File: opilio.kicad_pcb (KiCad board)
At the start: 4 copper layers, 74.9 x 40 mm, 92 parts, among them J1 Screw_Terminal_01x02, J2 USB_C_Receptacle_USB2.0, J3 Conn_01x02_Male, J4 Conn_01x02_Male, J5 Conn_01x02_Male, Q1 PMV25ENEAR, Q2 AO3401A, SW1 Reset, SW2 Boot, U1 EUP3458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

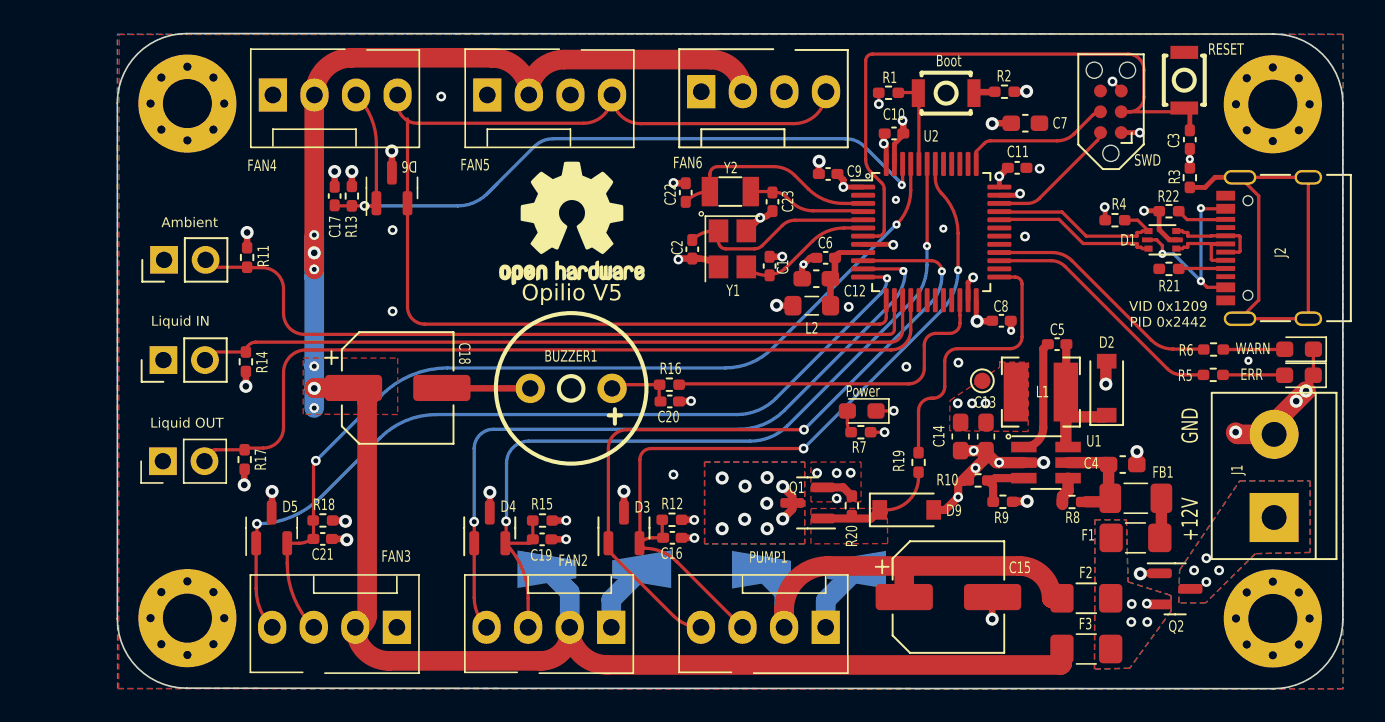
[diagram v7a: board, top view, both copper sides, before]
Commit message: v6 with P-channel mosfet
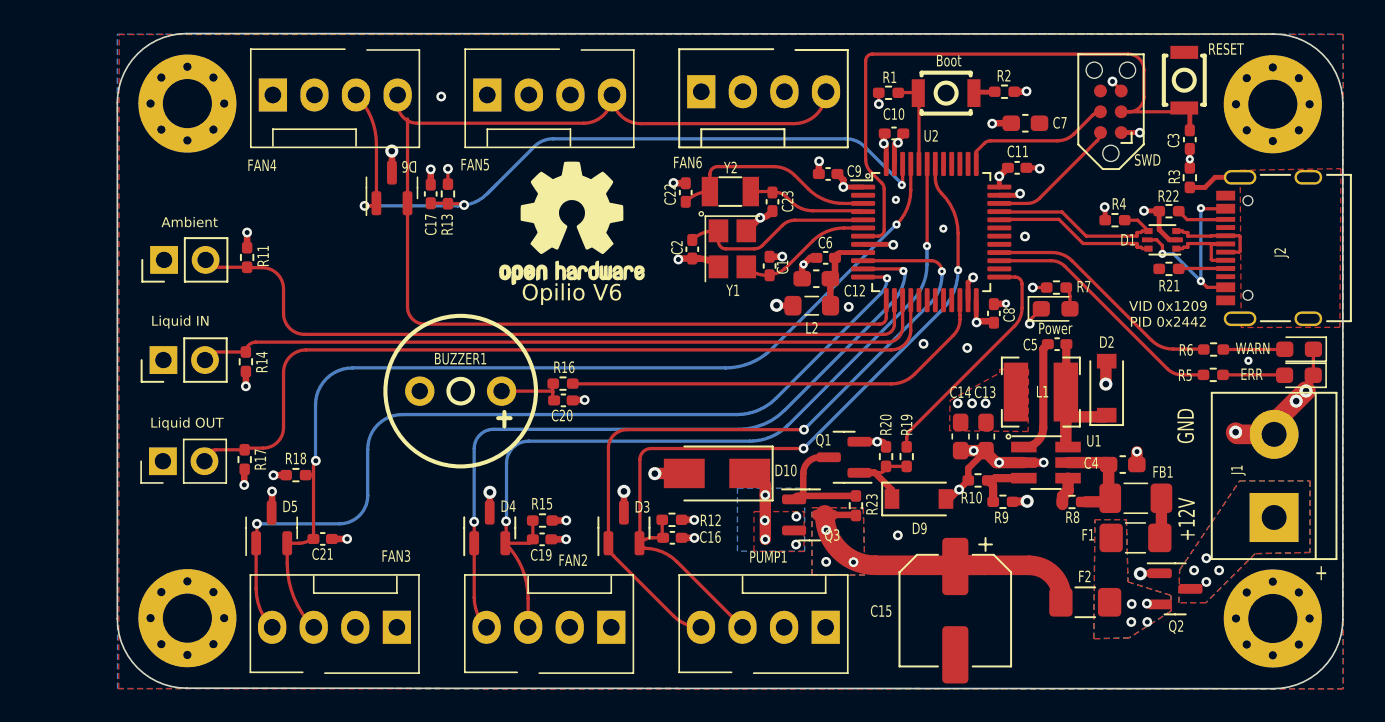
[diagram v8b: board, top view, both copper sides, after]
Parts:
- removed C18: 220uF, Capacitor_SMD:CP_Elec_6.3x7.7
- removed D8: B5819W, Diode_SMD:D_SMA-SMB_Universal_Handsoldering
- removed F3: 1.1A, Fuse:Fuse_1206_3216Metric_Pad1.42x1.75mm_HandSolder
- removed TP1: 3v3, TestPoint:TestPoint_Pad_D1.0mm
- added Q3: AO3401A, Package_TO_SOT_SMD:SOT-23, F.Cu at (147.4, 129.4)
- added R23: 10K, Resistor_SMD:R_0402_1005Metric_Pad0.72x0.64mm_HandSolder, F.Cu at (150.2, 128.8)
- D10: value B5819W -> B230A; footprint Diode_SMD:D_SMA-SMB_Universal_Handsoldering -> Diode_SMD:D_SMA; moved to F.Cu
- F2: value 2A -> 3A
- R20: value 7K5 -> 10K
- moved R7 14.9 mm to (162.5, 115.5), turned to 0 degrees
- moved Power1 13.4 mm to (162.4, 116.8), turned to 0 degrees
- moved D10 8.13 mm to (141.8, 126.8), turned to 180 degrees
- moved BUZZER1 6.75 mm to (126.1, 121.8)
- moved C20 6.50 mm to (132.4, 122.4)
- moved R16 6.50 mm to (132.3, 121.4)
- moved C17 5.87 mm to (124.3, 109.8)
- moved R13 5.87 mm to (125.3, 109.8)
- moved G*** 5.04 mm to (119.0, 128.4)
- moved R20 3.66 mm to (152.1, 125.8)
- moved Q1 3.57 mm to (149.5, 125.9)
- moved R18 3.22 mm to (116.0, 127.0), turned to 0 degrees
- moved D9 1.00 mm to (154.1, 128.4)
- moved C15 0.93 mm to (156.3, 135.2), turned to -90 degrees
- moved R19 0.81 mm to (153.3, 125.8)
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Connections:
- C15 pad 1: +12VF(P) -> +12VF(F)
- D10 pad 1: +12VF(P) -> 12vC
- D10 pad 2: D -> GND
- F2 pad 1: +12VF(P) -> +12VF(F)
- FAN2 pad 1: D -> GND
- FAN2 pad 2: +12VF(F) -> 12vC
- FAN3 pad 1: D -> GND
- FAN3 pad 2: +12VF(F) -> 12vC
- FAN4 pad 1: D -> GND
- FAN4 pad 2: +12VF(F) -> 12vC
- FAN5 pad 1: D -> GND
- FAN5 pad 2: +12VF(F) -> 12vC
- FAN6 pad 1: D -> GND
- FAN6 pad 2: +12VF(F) -> 12vC
- PUMP1 pad 1: D -> GND
- PUMP1 pad 2: +12VF(P) -> 12vC
- Q1 pad 3: D -> Net-(Q1-Pad3)
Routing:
- net +12VF(F): track 121.3 -> 20.8 mm, vias 6 -> 3
- net +12VF(P): track 26.7 -> 0.00 mm
- net Net-(J2-PadS1): track 29.9 -> 3.33 mm
- net D: track 11.1 -> 0.00 mm, vias 9 -> 0
- net Net-(Q1-Pad3): track 0.00 -> 7.75 mm
- net GND: track 63.9 -> 57.6 mm, vias 53 -> 47
- net BUZZER: track 21.2 -> 26.6 mm
- net 12vC: track 0.00 -> 4.45 mm, vias 0 -> 5
- net PWM_READ3: track 56.8 -> 59.9 mm
- net PWM_OUT3: track 52.2 -> 54.9 mm
- net FET_GATE: track 16.5 -> 14.4 mm
- net Net-(D9-Pad1): track 7.11 -> 6.29 mm
- net PWM_READ4: track 47.0 -> 47.2 mm, vias 2 -> 3
- added copper zone on B.Cu, net +12VF(F)
- added copper zone on B.Cu, net 12vC
- added copper zone on F.Cu, net 12vC
- added copper zone on In2.Cu, net 12vC
- added copper zone on F.Cu, net Net-(J2-PadS1)
- removed copper zone on B.Cu, net D
- removed copper zone on F.Cu, net D
- removed copper zone on In1.Cu, net D
- removed copper zone on F.Cu, net Net-(D9-Pad1)
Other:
- board text added: "+"
- board text added: "Opilio V6"
- board text removed: "Opilio V5"
